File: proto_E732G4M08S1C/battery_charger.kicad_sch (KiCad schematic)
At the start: 0 parts

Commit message: chg(pcb) battery charging
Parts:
- added C10: C, symbol Device:C
- added C11, C12: 4.7uF, symbol Device:C
- added J4: Conn_01x02_MountingPin, symbol Connector_Generic_MountingPin:Conn_01x02_MountingPin
- added LED1: orange, symbol Device:LED
- added R10: 1k5, symbol Device:R
- added R11, R8, R9: R, symbol Device:R
- added R7: 47k, symbol Device:R
- added U8: BQ24075RGT, Package_DFN_QFN:VQFN-16-1EP_3x3mm_P0.5mm_EP1.6x1.6mm, symbol Battery_Management:BQ24075RGT
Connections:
- new net: R11.1, U8.1 (TS)
- new net: R8.1, U8.12 (ILIM)
- new net: R7.1, U8.14 (TMR)
- new net: R9.1, U8.16 (ISET)
- new net: R10.2, U8.9 (~{CHG})
- new net: LED1.1 (K), R10.1
- new net +5V: C10.1, U8.13 (IN)
- new net +BATT: C11.1, J4.1 (Pin_1), U8.2 (BAT), U8.3 (BAT)
- new net GND: C10.2, C11.2, C12.2, J4.2 (Pin_2), J4.MP (MountPin), R11.2, R7.2, R8.2, R9.2, U8.17 (VSS), U8.8 (VSS)
- new net SYSOFF: U8.15 (SYSOFF)
- new net VCC: C12.1, LED1.2 (A), U8.10 (OUT), U8.11 (OUT)
- no-connect marks 0 -> 1

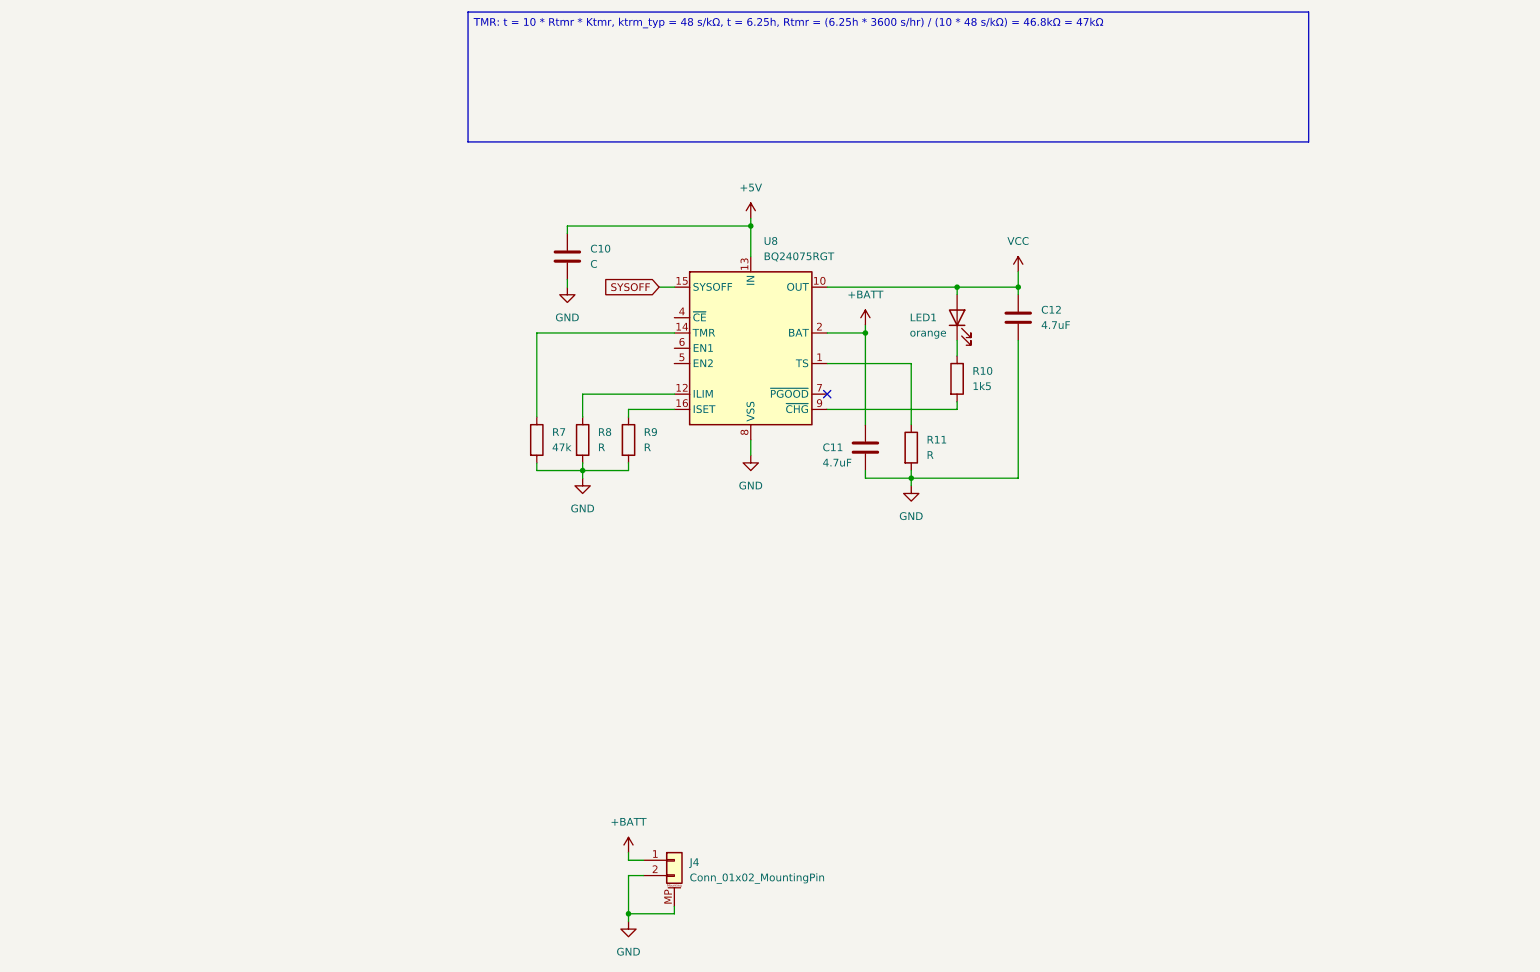
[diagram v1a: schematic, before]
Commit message: chg(pcb) more battery charger
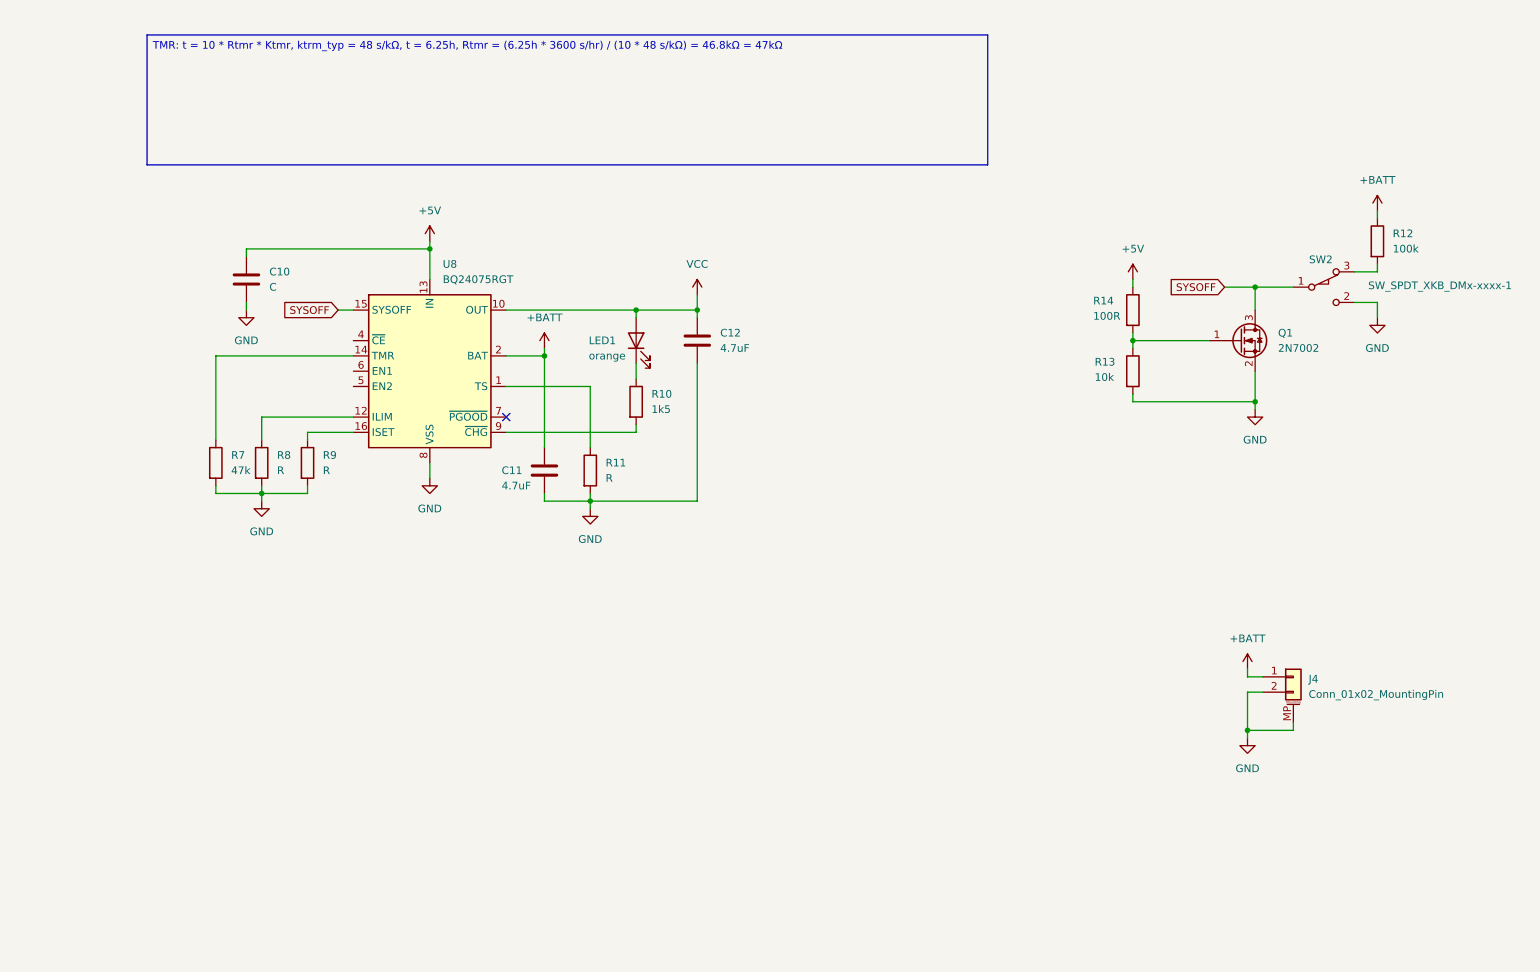
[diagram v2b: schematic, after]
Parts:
- added Q1: 2N7002, Package_TO_SOT_SMD:SOT-23, symbol Transistor_FET:2N7002
- added R12: 100k, symbol Device:R
- added R13: 10k, symbol Device:R
- added R14: 100R, symbol Device:R
- added SW2: SW_SPDT_XKB_DMx-xxxx-1, symbol Switch:SW_SPDT_XKB_DMx-xxxx-1
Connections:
- net +5V: now also R14.1
- net +BATT: now also R12.1
- net GND: now also Q1.2 (S), R13.2, SW2.2 (B)
- net SYSOFF: now also Q1.3 (D), SW2.1 (A)
- new net: Q1.1 (G), R13.1, R14.2
- new net: R12.2, SW2.3 (C)
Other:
- moved on the sheet: C10, C11, C12, J4, LED1, R10, R11, R7, R8, R9, U8

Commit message: feat(pcb) more changes
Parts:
- added R15, R16: 10k, Resistor_SMD:R_0603_1608Metric, symbol Device:R
- added TP1: I_{LIM}, TestPoint:TestPoint_Pad_D1.0mm, symbol Connector:TestPoint
- added TP2: SYSOFF, TestPoint:TestPoint_Pad_D1.0mm, symbol Connector:TestPoint
- added TP3: +VSW, TestPoint:TestPoint_Pad_D1.0mm, symbol Connector:TestPoint
- added TP4: +BATT, TestPoint:TestPoint_Pad_D1.0mm, symbol Connector:TestPoint
- added TP5: I_{max} EN1, TestPoint:TestPoint_Pad_D1.0mm, symbol Connector:TestPoint
- added TP6: I_{max} EN2, TestPoint:TestPoint_Pad_D1.0mm, symbol Connector:TestPoint
- C10: value C -> 4.7uF; footprint (none) -> Capacitor_SMD:C_0603_1608Metric
- C11, C12: footprint (none) -> Capacitor_SMD:C_0603_1608Metric
- J4: value Conn_01x02_MountingPin -> Battery
- R10, R12, R13, R14, R7: footprint (none) -> Resistor_SMD:R_0603_1608Metric
- R11: value R -> 10k; footprint (none) -> Resistor_SMD:R_0603_1608Metric
- R8: value R -> 1.33k; footprint (none) -> Resistor_SMD:R_0603_1608Metric
- R9: value R -> Rlim; footprint (none) -> Resistor_SMD:R_0603_1608Metric
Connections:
- net +BATT: now also TP4.1
- net GND: now also R7.1, R8.1, U8.4 (~{CE}), R15.2, R16.2; no longer R7.2, R8.2
- net SYSOFF: now also TP2.1
- net I_{LIM}: now reaches U8.12 (ILIM)
- net I_{LIM}: now also R8.2, TP1.1; no longer R8.1
- net at U8.14 (TMR): now also R7.2; no longer R7.1
- net I_{SET}: now reaches R9.1, U8.16 (ISET)
- net Imax_en2: now reaches U8.5 (EN2)
- net Imax_en2: now also R15.1, TP6.1
- net Imax_en1: now reaches U8.6 (EN1)
- net Imax_en1: now also R16.1, TP5.1
- net VCC renamed +VSW
- net +VSW: now also TP3.1
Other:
- moved on the sheet: R13, R14, R7, R8, R9
